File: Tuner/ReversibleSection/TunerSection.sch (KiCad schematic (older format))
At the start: 109 parts, among them J1 Conn_01x03, J10 Conn_01x02, J11 Conn_02x05_Odd_Even, J12 Conn_01x01, J13 Conn_01x01, J14 Conn_01x01, J15 Conn_01x01, J2 Conn_01x03, J3 Conn_01x03, J4 Conn_01x03, J5 Conn_01x03, J6 Conn_01x03, J7 Conn_01x03, J8 Conn_01x02, J9 Conn_01x02, P10 Conn_01x01, P11 Conn_01x01, P12 Conn_01x01, P2 Conn_01x01, P3 Conn_01x01, P4 Conn_01x01, P5 Conn_01x01, P6 Conn_01x01, P7 Conn_01x01, P8 Conn_01x01, P9 Conn_01x01, U1 MCP23008, U2 ULN2803A

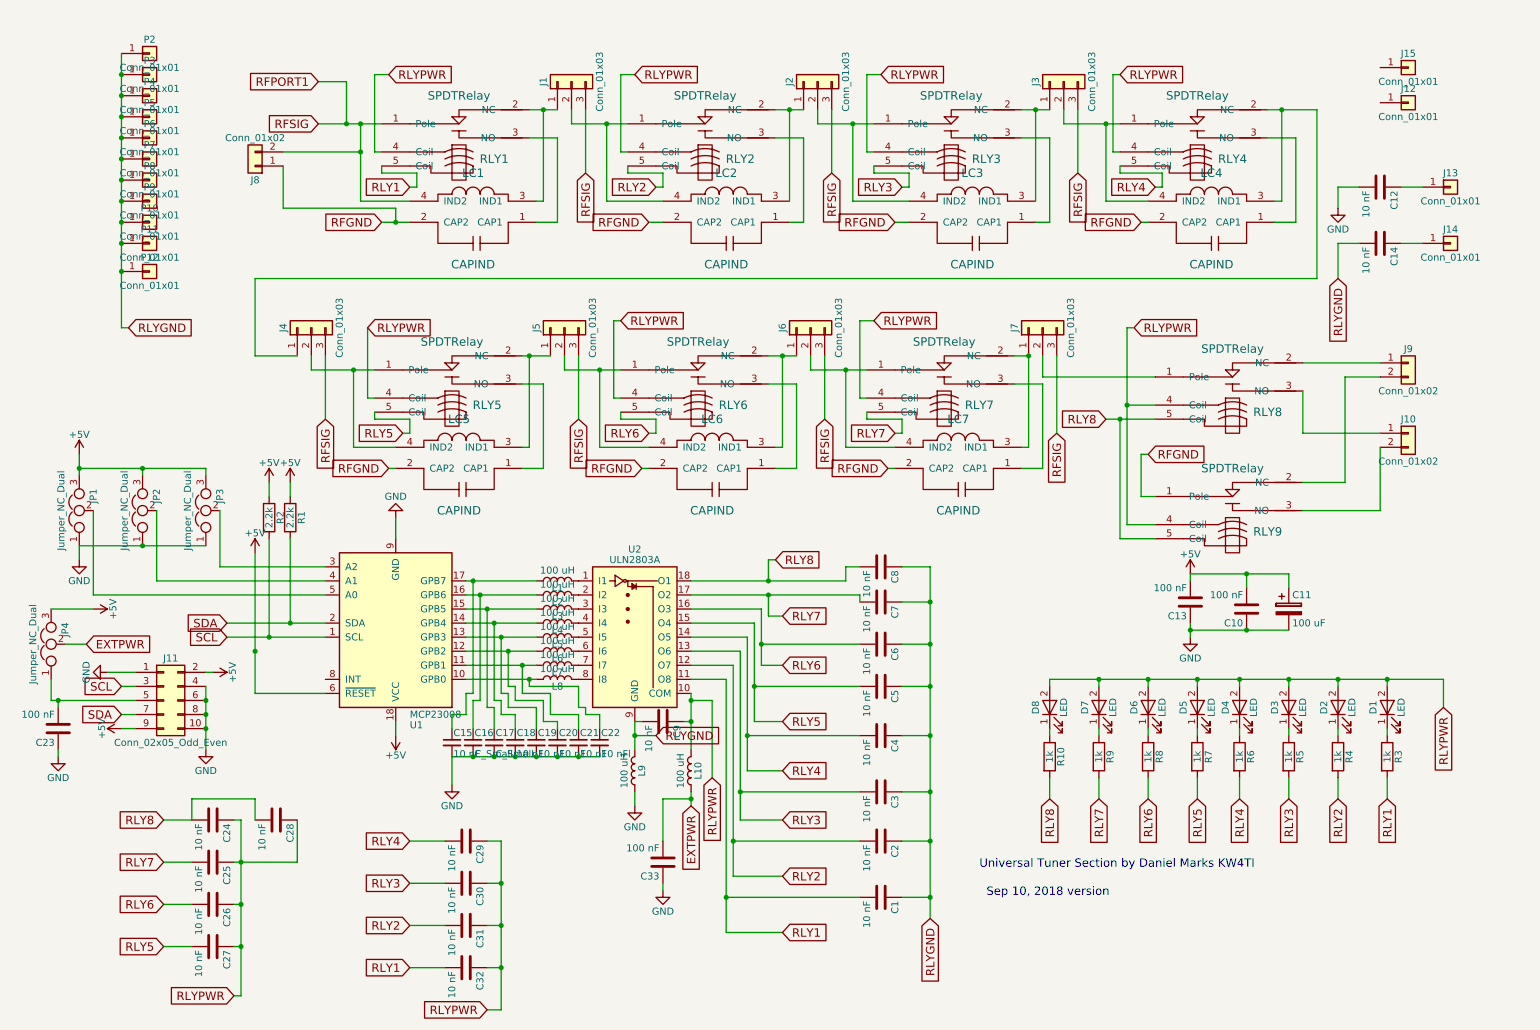
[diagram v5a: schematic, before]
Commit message: Added boards for SMIH/Schrack Relays
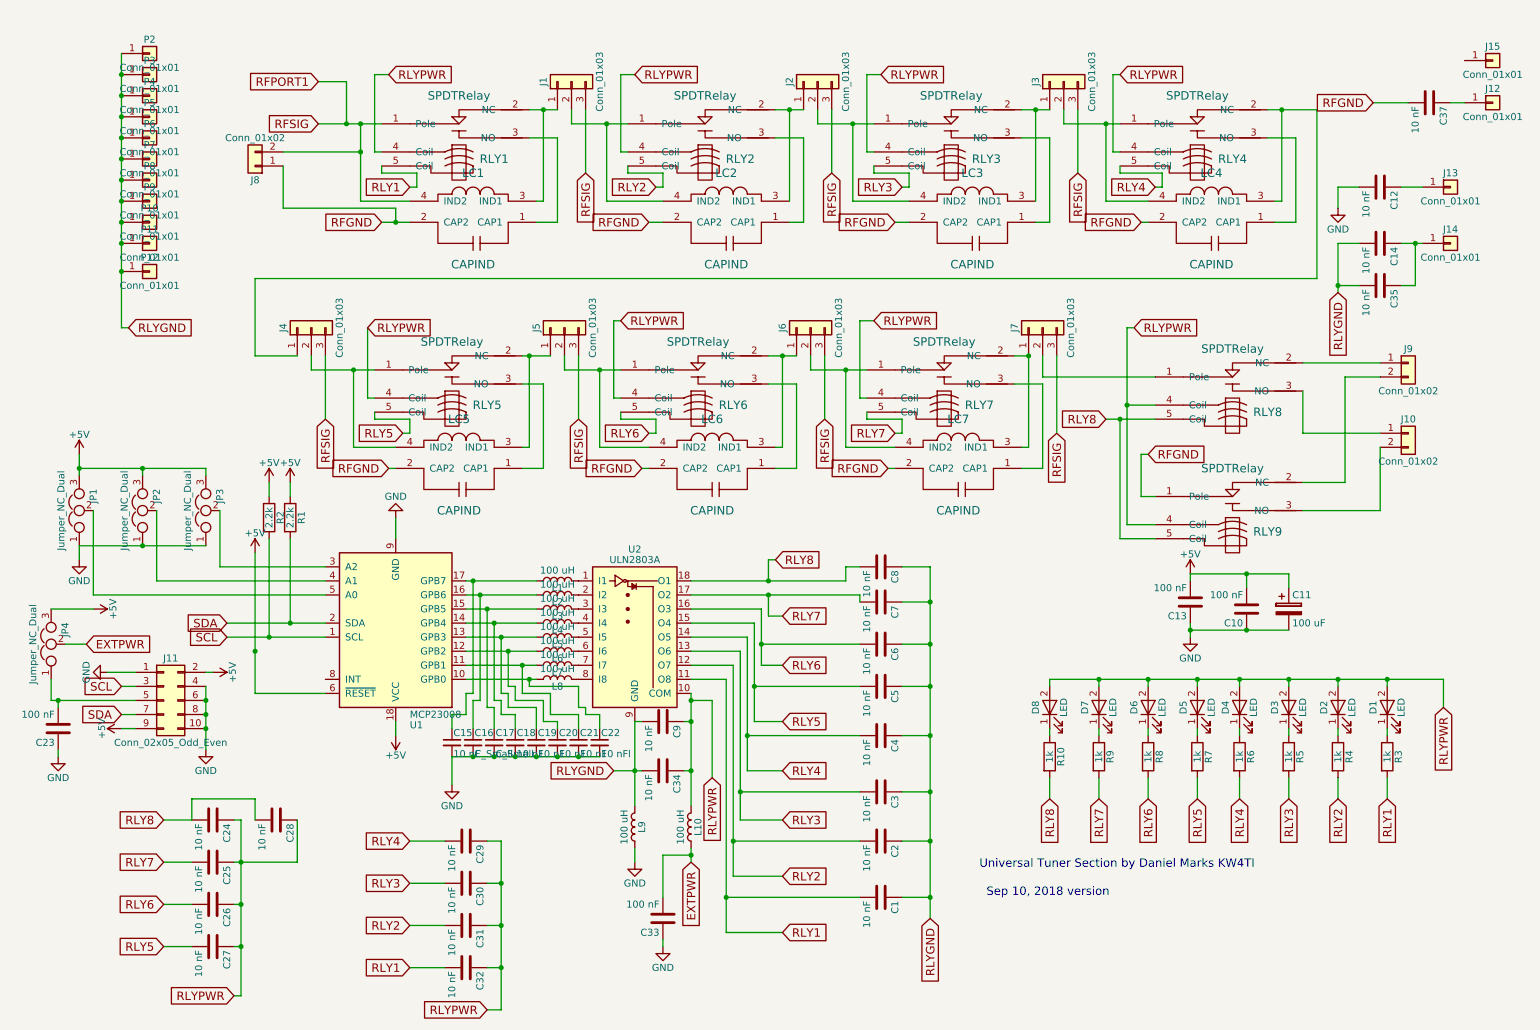
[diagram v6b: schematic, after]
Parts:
- added C34, C35, C37: 10 nF, Capacitors_THT:C_Disc_D5.0mm_W2.5mm_P5.00mm, symbol C
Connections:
- net RFGND: now also C37.2
- net RLYGND: now also C34.2, C35.2
- net RLYPWR: now also C34.1
- net at J12.1 (Pin_1): now also C37.1
- net at C14.1, J14.1 (Pin_1): now also C35.1
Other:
- moved on the sheet: C33, J12, J15, L10, L9
